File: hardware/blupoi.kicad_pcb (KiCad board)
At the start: 2 copper layers, 505.1 x 22.2 mm, 209 parts, among them P1 MICRO-B-USB, P2 CONN_02X05, SW1 PM_BTN, U1 NRF52832, U2 TPS63031DSKR, U3 bno055, U4 ics43432, U5 BQ24075RGTT, U6 MAX16054AZT+T, U7 CP2102-GMR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

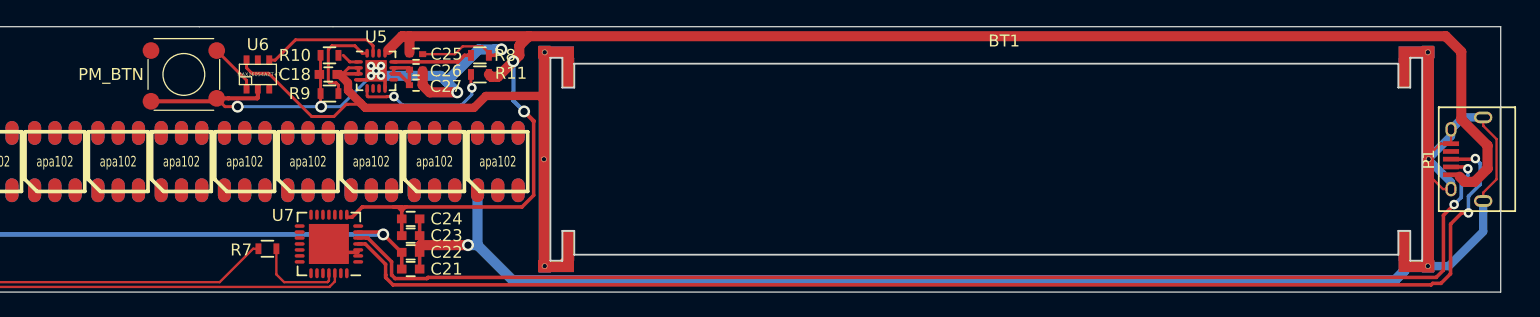
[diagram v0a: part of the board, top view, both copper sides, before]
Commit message: Changed to angled switch
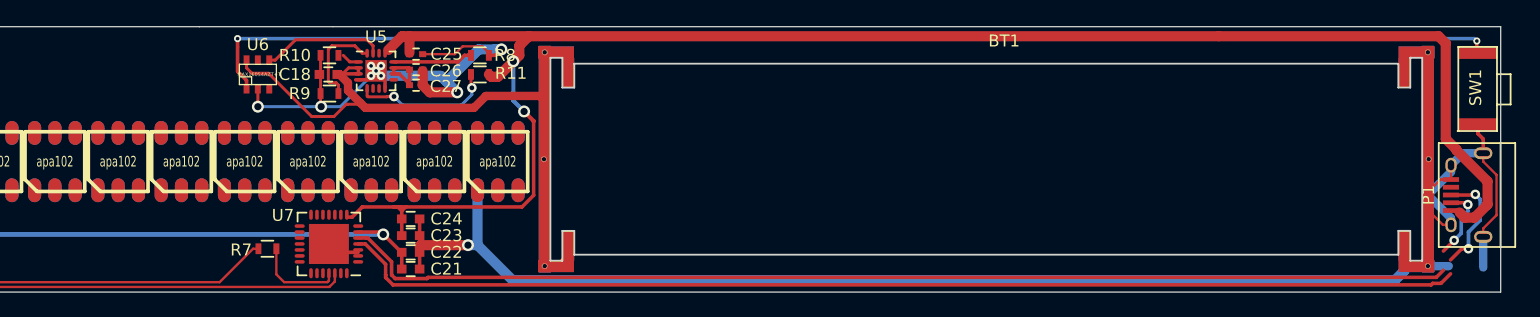
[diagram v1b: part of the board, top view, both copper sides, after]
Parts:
- SW1: footprint footprints:switch_spst_smd_5.5mm_4.5mm -> kss241glfs:KSS241GLFS
- moved SW1 106.9 mm to (434.2, 107.9), turned to 90 degrees
- moved P1 3.00 mm to (435.2, 113.3)
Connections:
- P1 pad 6: (no net) -> GND
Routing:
- net PM_SWITCH: track 4.23 -> 109.4 mm, vias 0 -> 2
- net GND: track 362.8 -> 348.8 mm
- net USB_D-: track 104.1 -> 99.5 mm
- net USB_D+: track 107.2 -> 103.0 mm
- net VUSB: track 143.7 -> 146.3 mm

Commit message: Moved switch
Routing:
- net ACC_I2C_SCL: track 241.4 -> 251.7 mm, vias 0 -> 2
- net ACC_I2C_SDA: track 241.0 -> 251.0 mm, vias 0 -> 4
- net Net-(LED0_16-Pad5): track 0.00 -> 8.43 mm
- net (no net): track 138.8 -> 130.9 mm
- net GND: track 348.8 -> 356.7 mm
- net Net-(LED0_16-Pad6): track 0.00 -> 7.82 mm
- net Net-(ANT2-Pad2): track 31.3 -> 29.6 mm
- net Net-(ANT2-Pad1): track 27.8 -> 26.9 mm

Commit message: Router all APA102 signal traces
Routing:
- net Net-(LED1_52-Pad5): track 0.00 -> 8.90 mm
- net Net-(LED1_44-Pad5): track 0.00 -> 8.87 mm
- net Net-(LED1_22-Pad5): track 0.00 -> 8.87 mm
- net Net-(LED1_40-Pad5): track 0.00 -> 8.87 mm
- net Net-(LED1_30-Pad5): track 0.00 -> 8.87 mm
- net Net-(LED1_25-Pad5): track 0.00 -> 8.87 mm
- net Net-(LED1_21-Pad5): track 0.00 -> 8.87 mm
- net Net-(LED1_17-Pad5): track 0.00 -> 8.87 mm
- net Net-(LED1_48-Pad5): track 0.00 -> 8.87 mm
- net Net-(LED1_33-Pad5): track 0.00 -> 8.87 mm
- net Net-(LED1_65-Pad5): track 0.00 -> 8.84 mm
- net Net-(LED1_60-Pad5): track 0.00 -> 8.84 mm
- net Net-(LED1_73-Pad5): track 0.00 -> 8.84 mm
- net Net-(LED1_61-Pad5): track 0.00 -> 8.84 mm
- net Net-(LED1_47-Pad5): track 0.00 -> 8.81 mm
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
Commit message: Route APA102 VIN traces
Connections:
- U1 pad 14: (no net) -> PM_ISET
- U1 pad 15: (no net) -> PM_EN1
- U1 pad 16: (no net) -> PM_EN2
- U1 pad 17: (no net) -> PM_!GOOD
- U1 pad 18: (no net) -> PM_!CHG
- U1 pad 19: (no net) -> PM_SWITCH
- U5 pad 6: (no net) -> PM_EN1
- U5 pad 7: (no net) -> PM_!GOOD
- U5 pad 9: (no net) -> PM_!CHG
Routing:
- net VIN: track 37.8 -> 661.5 mm, vias 2 -> 77
- net GND: track 356.7 -> 777.9 mm, vias 18 -> 22
- net APA102_1_MOSI: track 0.00 -> 6.99 mm, vias 0 -> 1
- net APA102_0_MOSI: track 0.00 -> 5.76 mm
- net APA102_1_SCK: track 0.00 -> 5.39 mm, vias 0 -> 1
- net APA102_0_SCK: track 0.00 -> 2.89 mm
- net USB_D-: track 99.5 -> 101.1 mm
- net USB_D+: track 103.0 -> 104.2 mm
- net Net-(LED1_17-Pad5): track 8.87 -> 7.82 mm

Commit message: WIP
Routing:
- net VIN: track 661.5 -> 668.0 mm, vias 77 -> 78
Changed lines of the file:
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@@
     (thickness 1.6)
     (drawings 10)
-    (tracks 3033)
+    (tracks 3045)
     (zones 0)
     (modules 209)
@@
   (segment (start -10.1 118.3) (end -14.2 114.2) (width 0.2) (layer F.Cu) (net 325))
   (segment (start -10 118.3) (end -10.1 118.3) (width 0.2) (layer F.Cu) (net 325))
+  (segment (start 344.658815 104.2) (end 345.432055 104.2) (width 0.25) (layer B.Cu) (net 326))
+  (segment (start 345.432055 104.2) (end 344.8 104.2) (width 0.25) (layer B.Cu) (net 326))
+  (segment (start 345.5 104.2) (end 345.432055 104.2) (width 0.25) (layer B.Cu) (net 326))
+  (segment (start 345.700001 104.400001) (end 345.5 104.2) (width 0.25) (layer B.Cu) (net 326))
+  (segment (start 346.4 104.8) (end 346.000001 104.400001) (width 0.25) (layer B.Cu) (net 326))
+  (segment (start 346.000001 104.400001) (end 345.700001 104.400001) (width 0.25) (layer B.Cu) (net 326))
+  (segment (start 346.4 104.1) (end 346.4 104.8) (width 0.25) (layer F.Cu) (net 326))
+  (segment (start 343.7 106.77499) (end 343.7 104.9) (width 0.25) (layer B.Cu) (net 326))
+  (segment (start 343.7 104.9) (end 344.4 104.2) (width 0.25) (layer B.Cu) (net 326))
+  (segment (start 344.4 104.2) (end 344.658815 104.2) (width 0.25) (layer B.Cu) (net 326))
+  (via (at 346.4 104.8) (size 0.8) (drill 0.4) (layers F.Cu B.Cu) (net 326))
+  (segment (start 343.7 106.77499) (end 345.92499 106.77499) (width 0.25) (layer B.Cu) (net 326))
+  (segment (start 342.37501 106.77499) (end 343.7 106.77499) (width 0.25) (layer B.Cu) (net 326))
   (segment (start 355.5 108.1) (end 355.5 107.65) (width 0.25) (layer F.Cu) (net 326))
   (segment (start 355.5 107.65) (end 354.62499 106.77499) (width 0.25) (layer F.Cu) (net 326))
@@
   (segment (start 341.5 108.1) (end 341.5 107.65) (width 0.25) (layer B.Cu) (net 326))
   (segment (start 341.5 107.65) (end 342.37501 106.77499) (width 0.25) (layer B.Cu) (net 326))
-  (segment (start 342.37501 106.77499) (end 345.92499 106.77499) (width 0.25) (layer B.Cu) (net 326))
   (segment (start 345.92499 106.77499) (end 346.8 107.65) (width 0.25) (layer B.Cu) (net 326))
   (segment (start 339.6 108.1) (end 339.6 107.787596) (width 0.25) (layer F.Cu) (net 326))

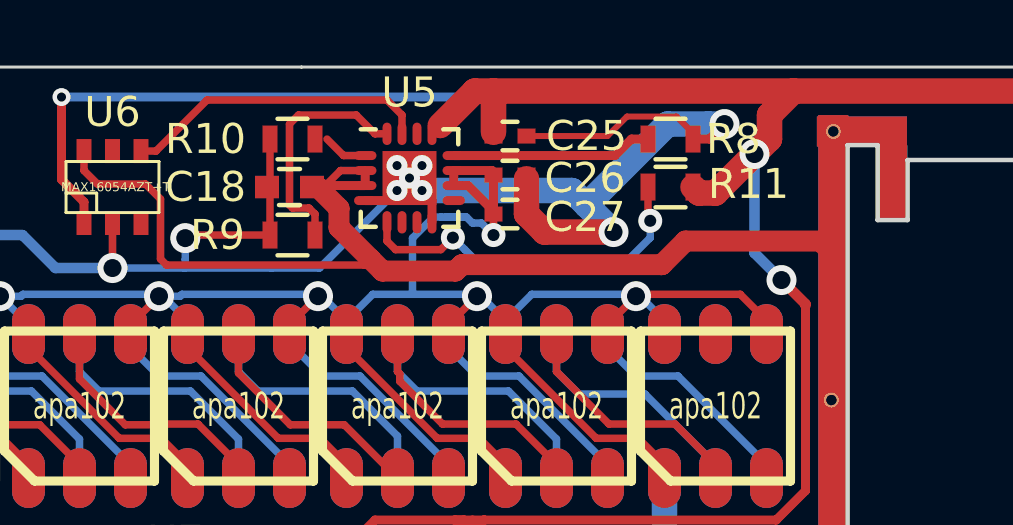
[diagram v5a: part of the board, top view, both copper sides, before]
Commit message: Small PMIC tweaks
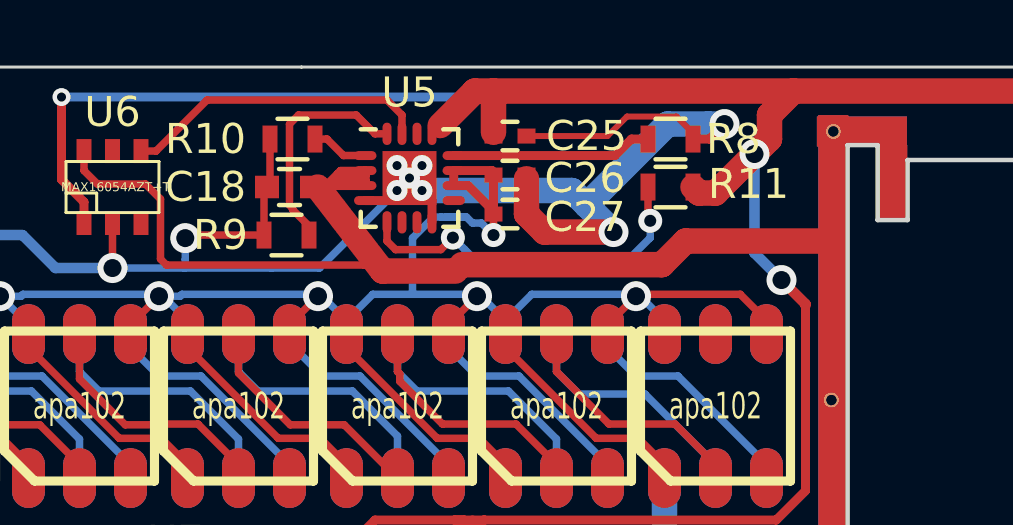
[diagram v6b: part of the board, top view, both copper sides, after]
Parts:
- moved R9 0.20 mm to (339.5, 104.8)
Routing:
- net VBAT: track 46.4 -> 49.2 mm
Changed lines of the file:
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@@
   (general
     (links 814)
-    (no_connects 192)
-    (area -67.365001 97.39772 441.0925 123.57622)
+    (no_connects 184)
+    (area -67.365001 99.149999 437.850001 121.480001)
     (thickness 1.6)
     (drawings 10)
-    (tracks 3045)
+    (tracks 3053)
     (zones 0)
     (modules 209)
@@
   )
   (module Resistors_SMD:R_0603 (layer F.Cu)
-    (at 339.7 104.8 180)
+    (at 339.5 104.8 180)
     (descr "Resistor SMD 0603, reflow soldering, Vishay (see dcrcw.pdf)")
     (tags "resistor 0603")
     (attr smd)
-    (fp_text reference R9 (at 2.5 0 180) (layer F.SilkS)
+    (fp_text reference R9 (at 2.2 0 180) (layer F.SilkS)
       (effects (font (size 1 1) (thickness 0.15)))
     )
@@
   (segment (start -33.75 120) (end -33.3 120) (width 0.2) (layer F.Cu) (net 1))
   (segment (start -34.300001 120.550001) (end -33.75 120) (width 0.2) (layer F.Cu) (net 1))
+  (segment (start 338.75 104.8) (end 338.75 103.3) (width 0.25) (layer F.Cu) (net 2))
+  (segment (start 338.75 103.3) (end 338.85 103.2) (width 0.25) (layer F.Cu) (net 2))
+  (segment (start 338.75 104.8) (end 336.227387 104.8) (width 0.25) (layer F.Cu) (net 2))
   (segment (start 336.227387 104.8) (end 336.12501 104.902377) (width 0.25) (layer F.Cu) (net 2))
   (segment (start 336.12501 105.87499) (end 336.12501 105.609483) (width 0.25) (layer B.Cu) (net 2))
   (segment (start 336.12501 105.609483) (end 336.12501 104.902377) (width 0.25) (layer B.Cu) (net 2))
   (segment (start 336.1 105.9) (end 336.12501 105.87499) (width 0.25) (layer B.Cu) (net 2))
-  (segment (start 338.95 104.8) (end 336.227387 104.8) (width 0.25) (layer F.Cu) (net 2))
   (via (at 336.12501 104.902377) (size 1) (drill 0.6) (layers F.Cu B.Cu) (net 2))
   (segment (start 339 105.9) (end 336.1 105.9) (width 0.25) (layer B.Cu) (net 2))
@@
   (segment (start 190.75 100.6875) (end 190.300001 100.6875) (width 0.4) (layer F.Cu) (net 2))
   (segment (start 191.25 100.6875) (end 190.75 100.6875) (width 0.4) (layer F.Cu) (net 2))
-  (segment (start 338.95 104.8) (end 338.95 103.3) (width 0.25) (layer F.Cu) (net 2))
   (segment (start 338.95 101.6) (end 338.95 103.1) (width 0.25) (layer F.Cu) (net 2))
   (segment (start 342.125 103.65) (end 341.9 103.65) (width 0.25) (layer F.Cu) (net 2))
@@
   (segment (start 346.35 102.65) (end 346.4 102.7) (width 0.3) (layer F.Cu) (net 326))
   (segment (start 345.075 103.15) (end 345.075 102.65) (width 0.3) (layer F.Cu) (net 326))
+  (segment (start 342.125 102.8) (end 342.125 103) (width 0.3) (layer F.Cu) (net 327))
+  (segment (start 342.125 102.65) (end 342.125 102.8) (width 0.3) (layer F.Cu) (net 327))
+  (segment (start 341.3 102.65) (end 341.2 102.75) (width 0.25) (layer F.Cu) (net 327))
+  (segment (start 341.2 102.75) (end 340.75 103.2) (width 0.25) (layer F.Cu) (net 327))
+  (segment (start 342.125 102.8) (end 341.25 102.8) (width 0.25) (layer F.Cu) (net 327))
+  (segment (start 341.25 102.8) (end 341.2 102.75) (width 0.25) (layer F.Cu) (net 327))
+  (segment (start 342.125 103) (end 342.125 103.15) (width 0.3) (layer F.Cu) (net 327))
+  (segment (start 342.125 103) (end 341.05 103) (width 0.25) (layer F.Cu) (net 327))
+  (segment (start 341.05 103) (end 340.9 103.15) (width 0.25) (layer F.Cu) (net 327))
+  (segment (start 342.1 105.8) (end 342.5 105.8) (width 0.25) (layer F.Cu) (net 327))
+  (segment (start 342.5 105.8) (end 342.7 106) (width 0.25) (layer F.Cu) (net 327))
   (segment (start 357.6635 109.946447) (end 357.6635 110.3) (width 0.7) (layer F.Cu) (net 327))
   (segment (start 357.3 105) (end 357.6635 105.3635) (width 0.7) (layer F.Cu) (net 327))
-  (segment (start 342.3 105.6) (end 342.7 106) (width 0.7) (layer F.Cu) (net 327))
-  (segment (start 342.7 106) (end 345.133592 106) (width 0.7) (layer F.Cu) (net 327))
-  (segment (start 352.8 105) (end 357.3 105) (width 0.7) (layer F.Cu) (net 327))
+  (segment (start 342.7 106) (end 345.133592 106) (width 0.85) (layer F.Cu) (net 327))
+  (segment (start 352.8 105) (end 357.3 105) (width 0.85) (layer F.Cu) (net 327))
   (segment (start 345.133592 106) (end 345.345998 105.787594) (width 0.7) (layer F.Cu) (net 327))
-  (segment (start 345.345998 105.787594) (end 352.012406 105.787594) (width 0.7) (layer F.Cu) (net 327))
-  (segment (start 352.012406 105.787594) (end 352.8 105) (width 0.7) (layer F.Cu) (net 327))
+  (segment (start 345.345998 105.787594) (end 352.012406 105.787594) (width 0.85) (layer F.Cu) (net 327))
+  (segment (start 352.012406 105.787594) (end 352.8 105) (width 0.85) (layer F.Cu) (net 327))
   (segment (start 357.6635 105.3635) (end 357.6635 109.946447) (width 0.7) (layer F.Cu) (net 327))
   (segment (start 332.75004 102.00112) (end 332.75004 102.65117) (width 0.25) (layer F.Cu) (net 327))
@@
   (segment (start 359.6955 118.2375) (end 358.6795 119.2535) (width 0.3) (layer F.Cu) (net 327))
   (segment (start 359.6955 103.061) (end 359.6955 102.3625) (width 0.3) (layer F.Cu) (net 327))
-  (segment (start 341.250001 104.550001) (end 342.3 105.6) (width 0.7) (layer F.Cu) (net 327))
+  (segment (start 340.540002 103.2) (end 342.7 106) (width 0.85) (layer F.Cu) (net 327))
   (segment (start 340.35 103.2) (end 340.540002 103.2) (width 0.7) (layer F.Cu) (net 327))
-  (segment (start 340.540002 103.2) (end 341.250001 103.909999) (width 0.7) (layer F.Cu) (net 327))
-  (segment (start 341.250001 103.909999) (end 341.250001 104.550001) (width 0.7) (layer F.Cu) (net 327))
   (segment (start 342.125 103.15) (end 340.9 103.15) (width 0.3) (layer F.Cu) (net 327))
   (segment (start 340.75 103.2) (end 340.775 103.2) (width 0.25) (layer F.Cu) (net 327))
   (segment (start 342.125 102.65) (end 341.3 102.65) (width 0.25) (layer F.Cu) (net 327))
-  (segment (start 341.3 102.65) (end 340.75 103.2) (width 0.25) (layer F.Cu) (net 327))
-  (segment (start 342.125 102.65) (end 342.125 103.15) (width 0.3) (layer F.Cu) (net 327))
   (segment (start -46.892894 114.6) (end -47.6 114.6) (width 0.5) (layer F.Cu) (net 328))
   (segment (start -42.807106 114.6) (end -42.957127 114.750021) (width 0.5) (layer F.Cu) (net 328))
@@
   (segment (start 350.45 102.15) (end 351 101.6) (width 0.3) (layer F.Cu) (net 333))
   (segment (start 345.075 102.15) (end 350.45 102.15) (width 0.3) (layer F.Cu) (net 333))
-  (segment (start 340.45 104.8) (end 340.45 104.1) (width 0.25) (layer F.Cu) (net 334))
-  (segment (start 340.45 104.1) (end 340.25 103.9) (width 0.25) (layer F.Cu) (net 334))
-  (segment (start 340.25 103.9) (end 339.7 103.9) (width 0.25) (layer F.Cu) (net 334))
+  (segment (start 339.7 103.9) (end 339.7 103.95) (width 0.25) (layer F.Cu) (net 334))
+  (segment (start 339.7 103.95) (end 340.35 104.6) (width 0.25) (layer F.Cu) (net 334))
+  (segment (start 340.35 104.6) (end 340.35 104.8) (width 0.25) (layer F.Cu) (net 334))
   (segment (start 339.7 103.9) (end 339.6 103.8) (width 0.25) (layer F.Cu) (net 334))
   (segment (start 339.6 101.1) (end 339.9 100.8) (width 0.25) (layer F.Cu) (net 334))
@@
   (segment (start 341.825 100.8) (end 342.45 101.425) (width 0.25) (layer F.Cu) (net 334))
   (segment (start 342.45 101.425) (end 342.85 101.425) (width 0.25) (layer F.Cu) (net 334))
+  (segment (start 340.85 101.6) (end 340.45 101.6) (width 0.25) (layer F.Cu) (net 335))
   (segment (start 342.125 102.15) (end 341.4 102.15) (width 0.25) (layer F.Cu) (net 335))
   (segment (start 341.4 102.15) (end 340.85 101.6) (width 0.25) (layer F.Cu) (net 335))

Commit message: WIP
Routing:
- net VIN: track 668.0 -> 789.0 mm
- net VBAT: track 49.2 -> 50.8 mm, vias 0 -> 2
- net GND: track 777.9 -> 779.0 mm, vias 22 -> 21
- net PM_SWITCH: track 109.4 -> 110.4 mm

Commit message: WIP
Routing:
- net VIN: track 789.0 -> 964.4 mm
